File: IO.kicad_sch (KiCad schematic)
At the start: 40 parts, among them J401 DMX_{IN}, J402 DMX_{THRU}, Q401 AO3400A, Q402 AO3400A, U401 6N137, U402 SN65176B, U403 6N137, U404 6N137, U405 AMS1117-5.0

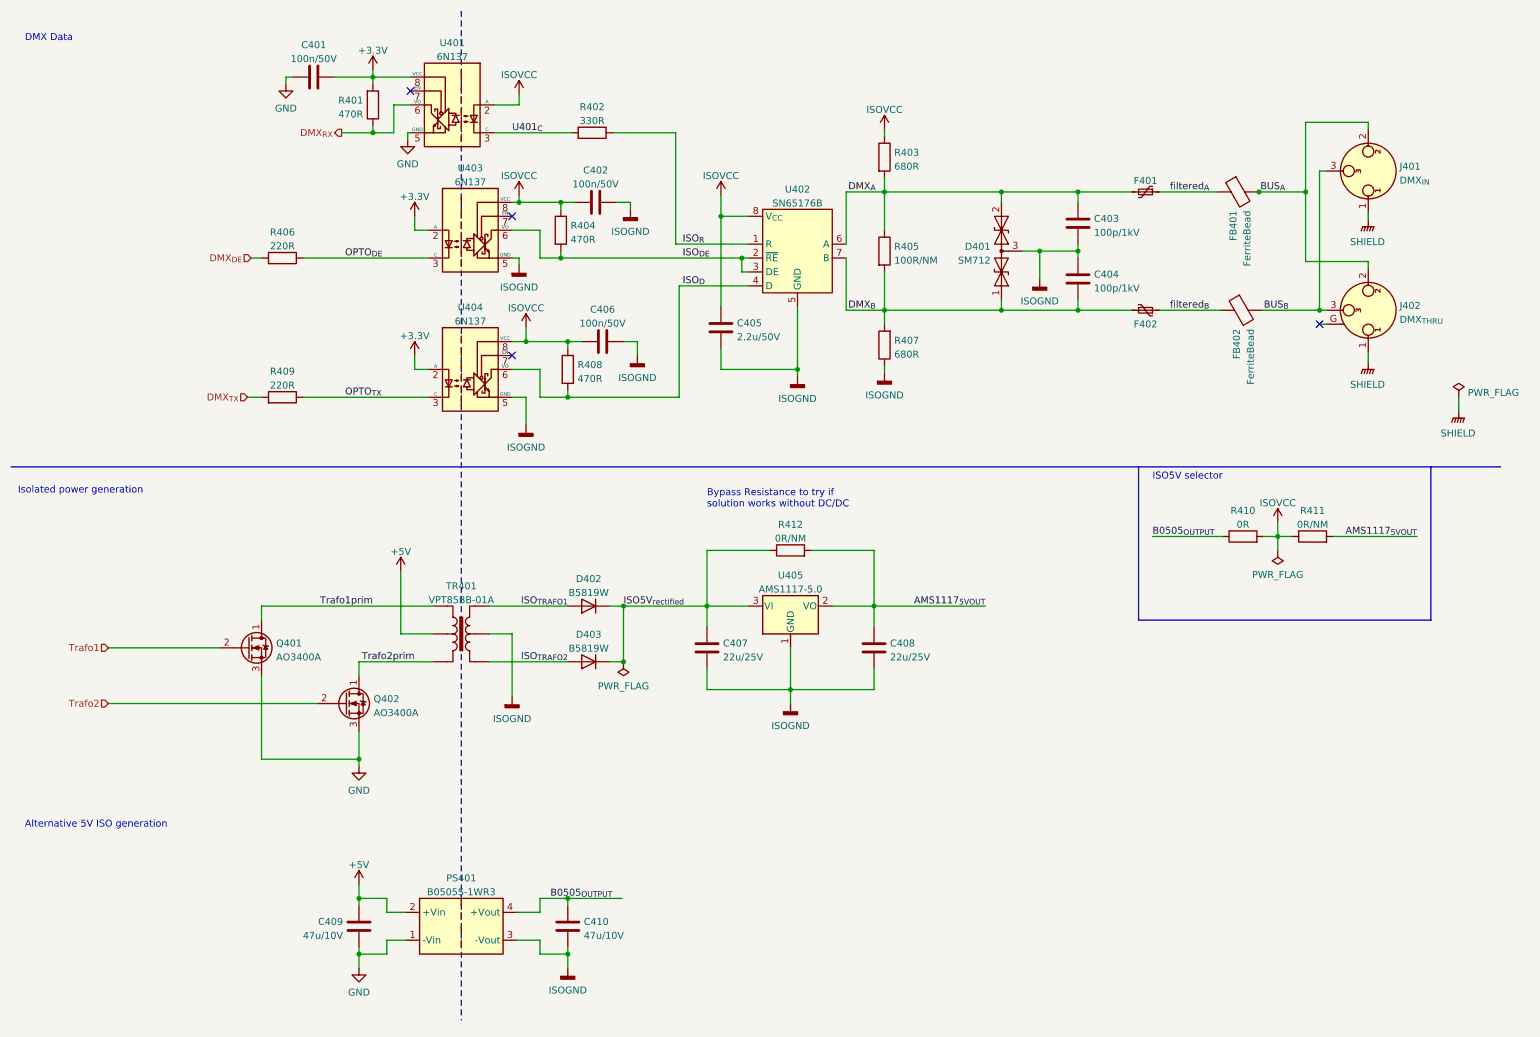
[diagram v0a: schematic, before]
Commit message: Added Testpoints
Schematic and PCB updated
Also probably some other smaller changes that I forgot about
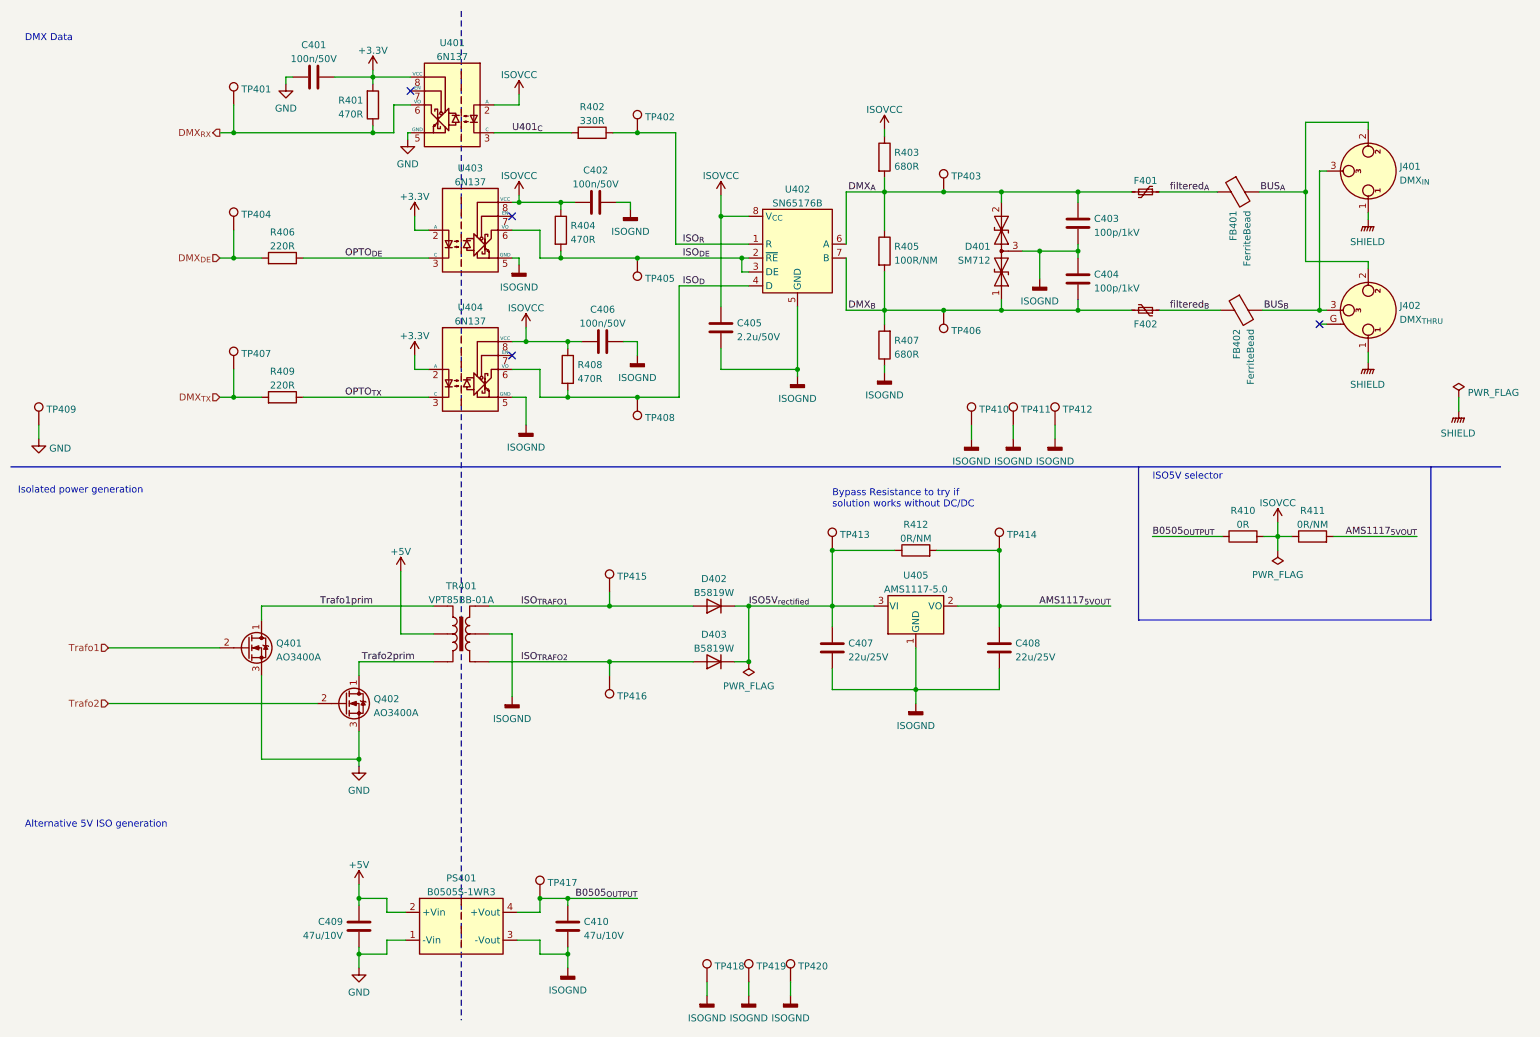
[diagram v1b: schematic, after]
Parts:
- added TP401, TP402, TP403, TP404, TP405, TP406, TP407, TP408, TP409, TP410, TP411, TP412, TP413, TP414, TP415, TP416, TP417, TP418, TP419, TP420: TestPoint, TestPoint:TestPoint_Loop_D1.80mm_Drill1.0mm_Beaded, symbol Connector:TestPoint
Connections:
- net AMS1117_{5VOUT}: now also TP414.1
- net B0505_{OUTPUT}: now also TP417.1
- net DMX_{A}: now also TP403.1
- net DMX_{B}: now also TP406.1
- net DMX_{DE}: now also TP404.1
- net DMX_{RX}: now also TP401.1
- net DMX_{TX}: now also TP407.1
- net GND: now also TP409.1
- net ISO5V_{rectified}: now also TP413.1
- net ISOGND: now also TP410.1, TP411.1, TP412.1, TP418.1, TP419.1, TP420.1
- net ISO_{DE}: now also TP405.1
- net ISO_{D}: now also TP408.1
- net ISO_{R}: now also TP402.1
- net ISO_{TRAFO1}: now also TP415.1
- net ISO_{TRAFO2}: now also TP416.1
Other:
- moved on the sheet: C407, C408, D402, D403, R412, U405

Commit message: Fix DRCs and BOM errors
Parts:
- R410: LCSC C17888 -> C17477
- R411, R412: footprint Resistor_SMD:R_1206_3216Metric_Pad1.30x1.75mm_HandSolder -> Resistor_SMD:R_0805_2012Metric; LCSC C17888 -> (none)
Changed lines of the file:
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@@
     (property "Reference" "R412" (id 0) (at 177.8 104.5042 90))
     (property "Value" "0R/NM" (id 1) (at 177.8 107.0411 90))
-    (property "Footprint" "Resistor_SMD:R_1206_3216Metric_Pad1.30x1.75mm_HandSolder" (id 2) (at 177.8 110.998 90)
+    (property "Footprint" "Resistor_SMD:R_0805_2012Metric" (id 2) (at 177.8 110.998 90)
       (effects (font (size 1.27 1.27)) hide)
     )
@@
       (effects (font (size 1.27 1.27)) hide)
     )
-    (property "LCSC" "C17888" (id 4) (at 177.8 109.22 90)
+    (property "LCSC" "" (id 4) (at 177.8 109.22 90)
       (effects (font (size 1.27 1.27)) hide)
     )
@@
     (property "Reference" "R411" (id 0) (at 250.19 101.9642 90))
     (property "Value" "0R/NM" (id 1) (at 250.19 104.5011 90))
-    (property "Footprint" "Resistor_SMD:R_1206_3216Metric_Pad1.30x1.75mm_HandSolder" (id 2) (at 250.19 108.458 90)
+    (property "Footprint" "Resistor_SMD:R_0805_2012Metric" (id 2) (at 250.19 108.458 90)
       (effects (font (size 1.27 1.27)) hide)
     )
@@
       (effects (font (size 1.27 1.27)) hide)
     )
-    (property "LCSC" "C17888" (id 4) (at 250.19 106.68 90)
+    (property "LCSC" "" (id 4) (at 250.19 106.68 90)
       (effects (font (size 1.27 1.27)) hide)
     )
@@
       (effects (font (size 1.27 1.27)) hide)
     )
-    (property "LCSC" "C17888" (id 4) (at 237.49 106.68 90)
-      (effects (font (size 1.27 1.27)) hide)
-    )
+    (property "LCSC" "C17477" (id 4) (at 237.49 106.68 90)
+      (effects (font (size 1.27 1.27)) hide)
+    )
